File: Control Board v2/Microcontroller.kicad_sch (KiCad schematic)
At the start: 0 parts

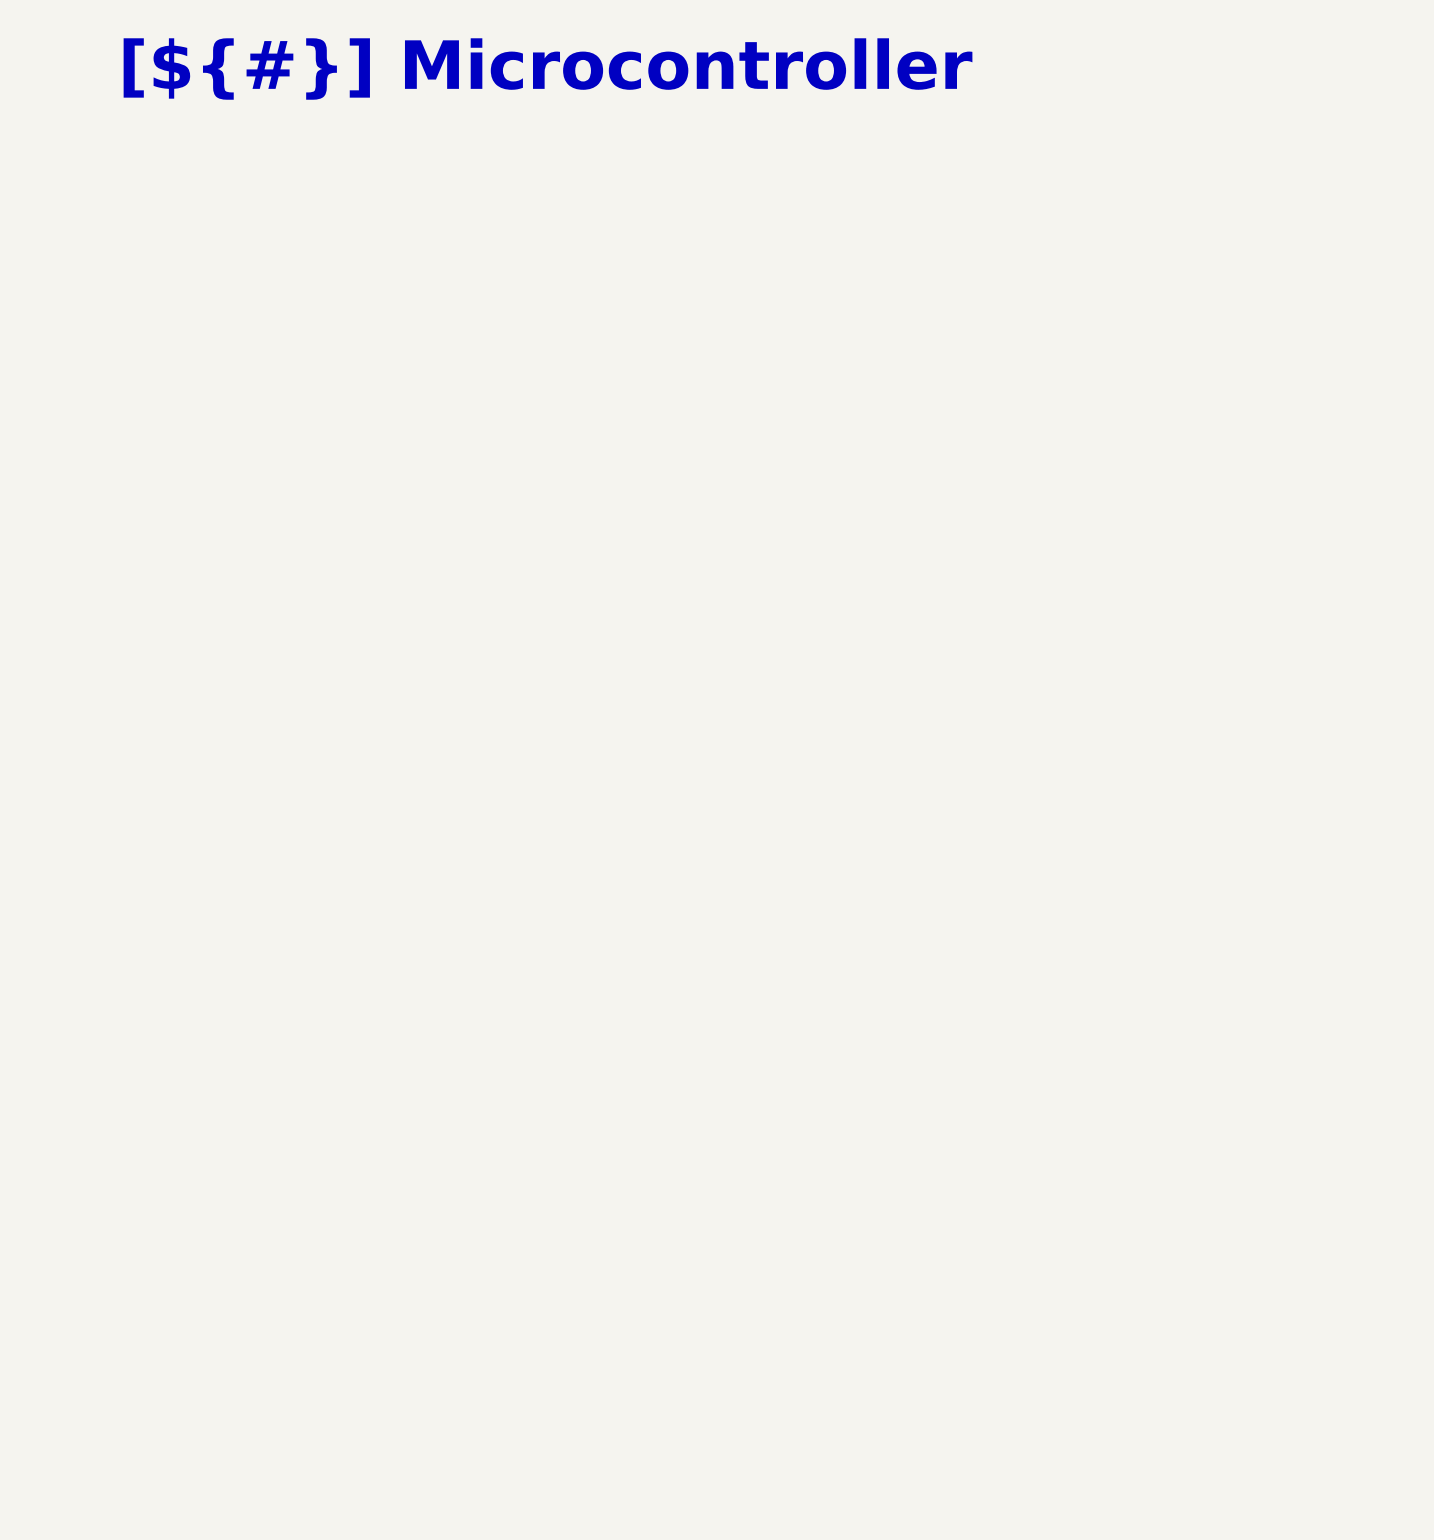
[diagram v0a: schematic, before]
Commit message: draft microcontroller and interface circuits, still need to finish interfaces
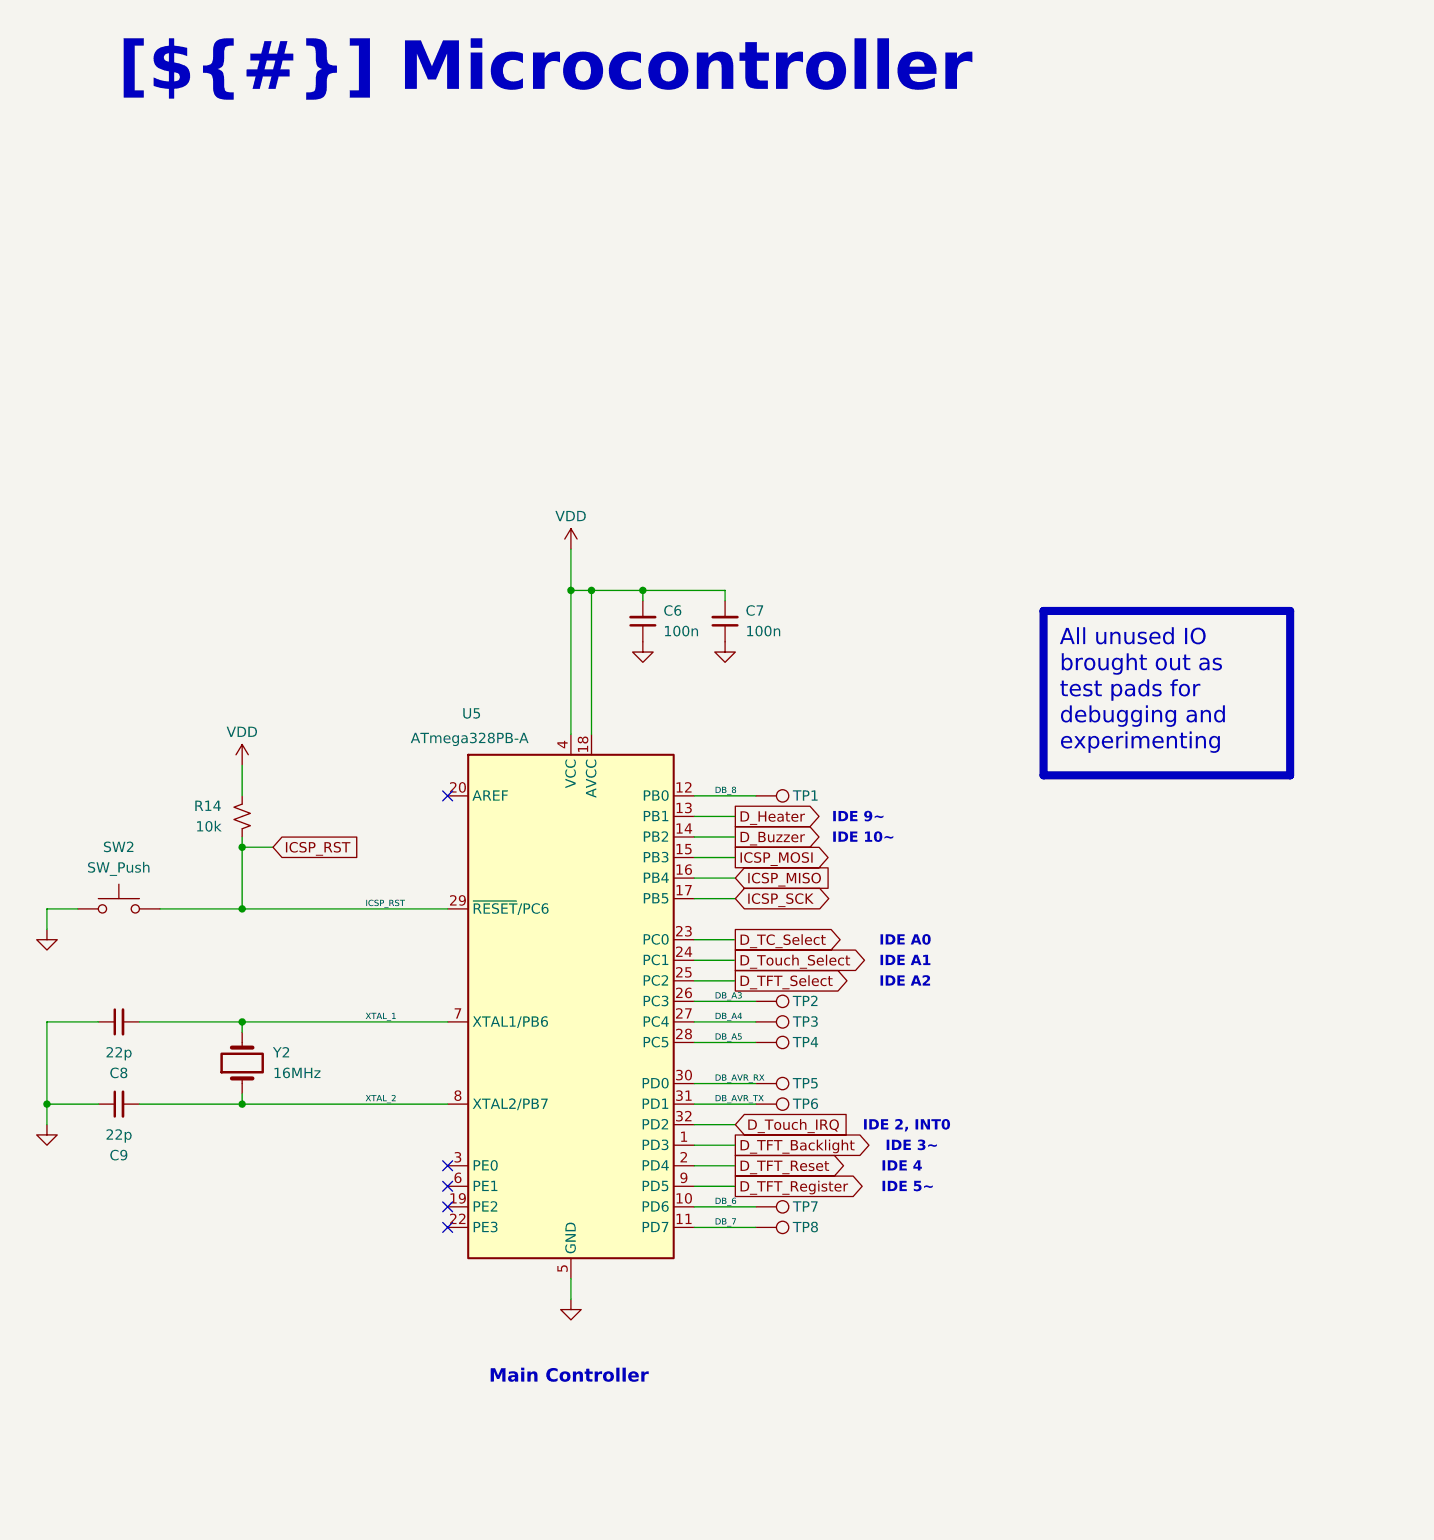
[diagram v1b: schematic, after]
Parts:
- added C6, C7: 100n, Capacitor_SMD:C_0402_1005Metric, symbol Device:C_Small
- added C8, C9: 22p, Capacitor_SMD:C_0402_1005Metric, symbol Device:C_Small
- added R14: 10k, Resistor_SMD:R_0402_1005Metric, symbol Device:R_Small_US
- added SW2: SW_Push, Button_Switch_THT:SW_Tactile_SPST_Angled_PTS645Vx58-2LFS, symbol Switch:SW_Push
- added TP1, TP2, TP3, TP4, TP5, TP6, TP7, TP8: TestPoint, symbol Connector:TestPoint
- added U5: ATmega328PB-A, Package_QFP:TQFP-32_7x7mm_P0.8mm, symbol MCU_Microchip_ATmega:ATmega328PB-A
- added Y2: 16MHz, Crystal:Crystal_SMD_3225-4Pin_3.2x2.5mm, symbol Device:Crystal
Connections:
- new net DB_6: TP7.1, U5.10 (PD6)
- new net DB_7: TP8.1, U5.11 (PD7)
- new net DB_8: TP1.1, U5.12 (PB0)
- new net DB_A3: TP2.1, U5.26 (PC3)
- new net DB_A4: TP3.1, U5.27 (PC4)
- new net DB_A5: TP4.1, U5.28 (PC5)
- new net DB_AVR_RX: TP5.1, U5.30 (PD0)
- new net DB_AVR_TX: TP6.1, U5.31 (PD1)
- new net D_Buzzer: U5.14 (PB2)
- new net D_Heater: U5.13 (PB1)
- new net D_TC_Select: U5.23 (PC0)
- new net D_TFT_Backlight: U5.1 (PD3)
- new net D_TFT_Register: U5.9 (PD5)
- new net D_TFT_Reset: U5.2 (PD4)
- new net D_TFT_Select: U5.25 (PC2)
- new net D_Touch_IRQ: U5.32 (PD2)
- new net D_Touch_Select: U5.24 (PC1)
- new net GND: C6.1, C7.1, C8.1, C9.1, SW2.1, U5.21 (GND), U5.5 (GND)
- new net ICSP_MISO: U5.16 (PB4)
- new net ICSP_MOSI: U5.15 (PB3)
- new net ICSP_RST: R14.1, SW2.2, U5.29 (~{RESET}/PC6)
- new net ICSP_SCK: U5.17 (PB5)
- new net VDD: C6.2, C7.2, R14.2, U5.18 (AVCC), U5.4 (VCC)
- new net XTAL_1: C8.2, U5.7 (XTAL1/PB6), Y2.2
- new net XTAL_2: C9.2, U5.8 (XTAL2/PB7), Y2.1
- no-connect marks 0 -> 5
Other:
- note added: "IDE 10~"
- note added: "IDE 2, INT0"
- note added: "IDE 3~"
- note added: "IDE 4"
- note added: "IDE 5~"
- note added: "IDE 9~"
- note added: "IDE A0"
- note added: "IDE A1"
- note added: "IDE A2"
- note added: "Main Controller"

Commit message: work on PCB layout
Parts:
- added D4: RED, LED_SMD:LED_0603_1608Metric_Pad1.05x0.95mm_HandSolder, symbol Device:LED_Filled
- added R8: 330, Resistor_SMD:R_0603_1608Metric_Pad0.98x0.95mm_HandSolder, symbol Device:R_US
- SW2: footprint Button_Switch_THT:SW_Tactile_SPST_Angled_PTS645Vx58-2LFS -> Button_Switch_THT:SW_TH_Tactile_Omron_B3F-102x
- TP1, TP2, TP3, TP4, TP5, TP6, TP7, TP8: footprint (none) -> TestPoint:TestPoint_Pad_D1.5mm
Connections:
- net DB_7: now also D4.2 (A)
- net GND: now also R8.2
- new net D4_K: D4.1 (K), R8.1
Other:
- moved on the sheet: TP8
